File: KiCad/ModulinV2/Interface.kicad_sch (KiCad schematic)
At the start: 57 parts, among them IC10 DAC60501ZDGSR, IC11 DAC60501ZDGSR, IC4 TL072HIDR, IC5 TL074HIDR, IC51 TL072HIDR, IC6 ADS7041IDCUR, IC7 ADS7041IDCUR, IC8 ADS7866IDBVT, IC9 ADS7866IDBVT

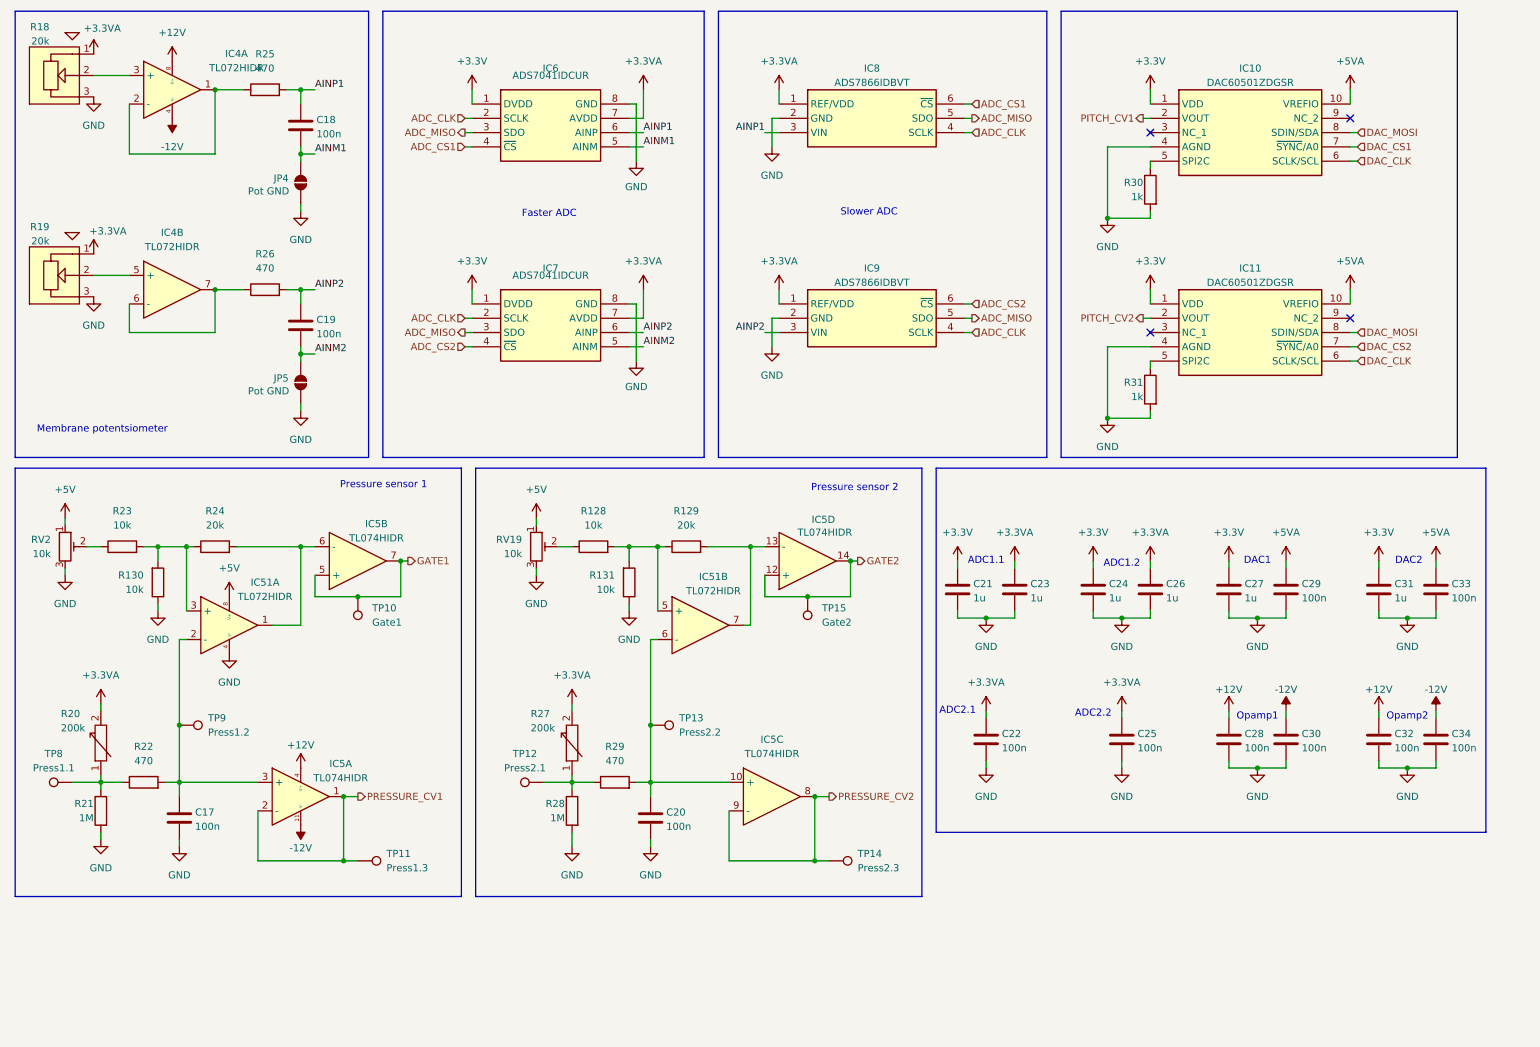
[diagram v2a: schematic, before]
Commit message: Started adding footprints for capacitors
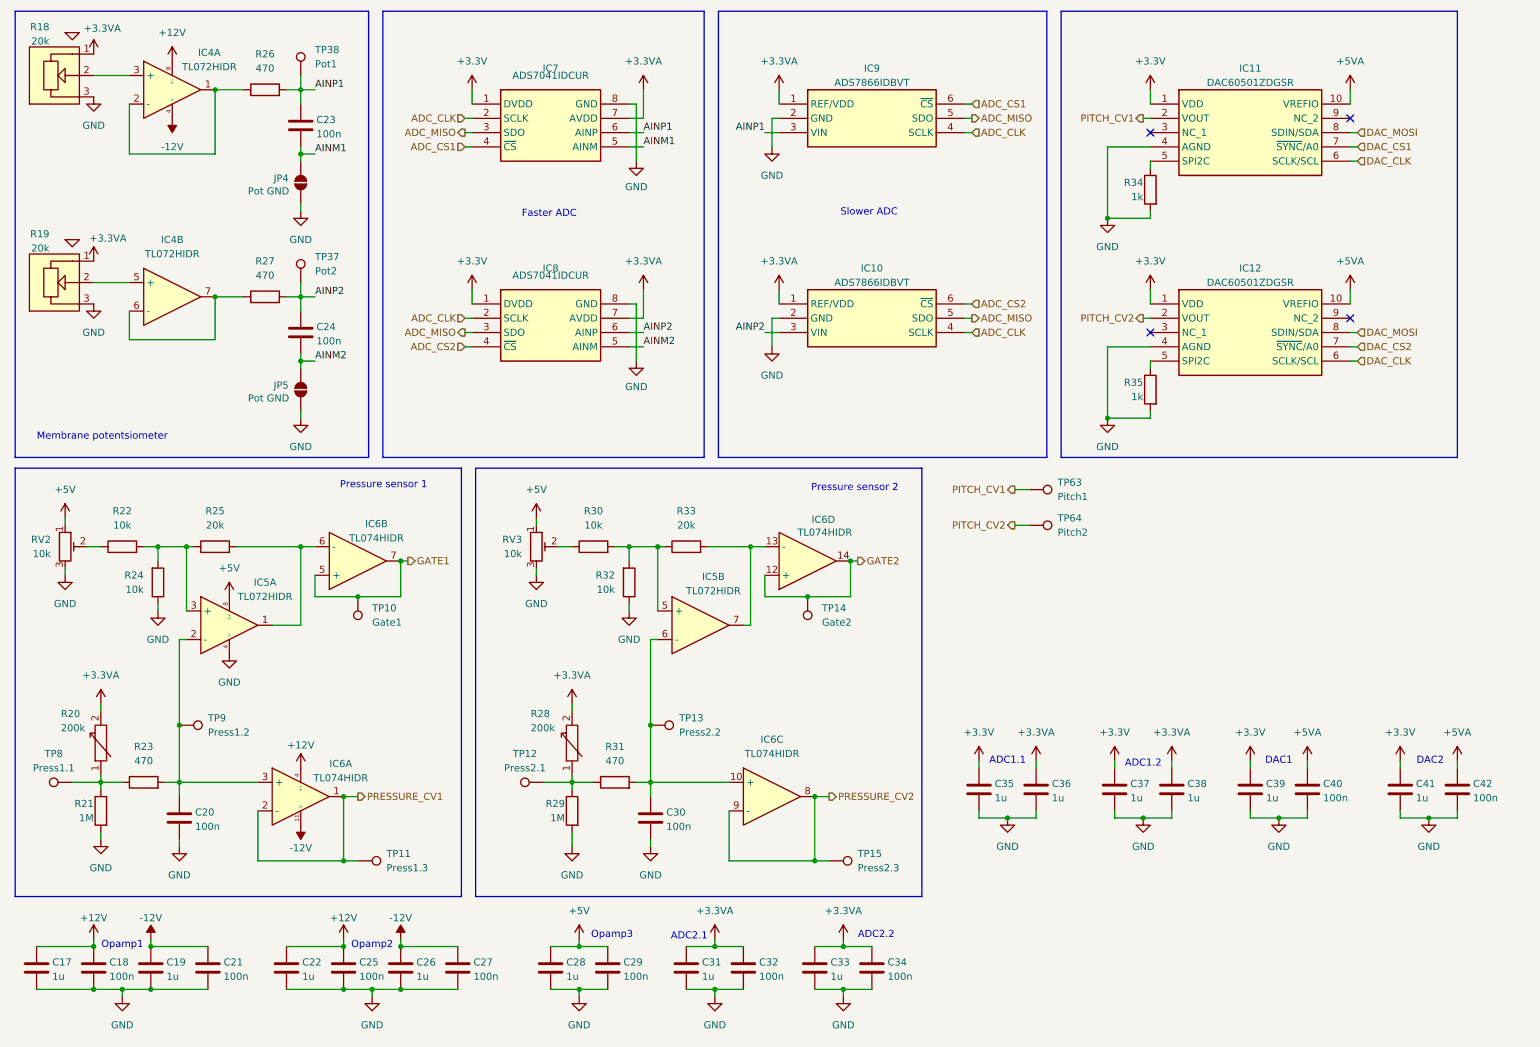
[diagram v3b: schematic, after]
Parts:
- removed C30, C34: 100n, symbol Device:C
- added C17, C19, C26, C31, C33: 1u, SamacSys_Parts:CAPC1608X95N, symbol Device:C
- added C18, C21, C25, C27, C29: 100n, SamacSys_Parts:CAPC1608X90N, symbol Device:C
- added TP37: Pot2, SamacSys_Parts:TestPointLoop, symbol Connector:TestPoint
- added TP38: Pot1, SamacSys_Parts:TestPointLoop, symbol Connector:TestPoint
- added TP63: Pitch1, SamacSys_Parts:TestPointLoop, symbol Connector:TestPoint
- added TP64: Pitch2, SamacSys_Parts:TestPointLoop, symbol Connector:TestPoint
- C20: renamed from C17; footprint (none) -> SamacSys_Parts:CAPC1608X90N
- C22, C28: value 100n -> 1u; footprint (none) -> SamacSys_Parts:CAPC1608X95N
- C23: renamed from C18; footprint (none) -> SamacSys_Parts:CAPC1608X90N
- C24: renamed from C19; footprint (none) -> SamacSys_Parts:CAPC1608X90N
- C30: renamed from C20; footprint (none) -> SamacSys_Parts:CAPC1608X90N
- C32: footprint (none) -> SamacSys_Parts:CAPC1608X90N
- C34: renamed from C25; footprint (none) -> SamacSys_Parts:CAPC1608X90N
- C35: renamed from C21; footprint (none) -> SamacSys_Parts:CAPC1608X95N
- C36: renamed from C23; footprint (none) -> SamacSys_Parts:CAPC1608X95N
- C37: renamed from C24; footprint (none) -> SamacSys_Parts:CAPC1608X95N
- C38: renamed from C26; footprint (none) -> SamacSys_Parts:CAPC1608X95N
- C39: renamed from C27; footprint (none) -> SamacSys_Parts:CAPC1608X95N
- C40: renamed from C29; footprint (none) -> SamacSys_Parts:CAPC1608X90N
- C41: renamed from C31; footprint (none) -> SamacSys_Parts:CAPC1608X95N
- C42: renamed from C33; footprint (none) -> SamacSys_Parts:CAPC1608X90N
- TP10, TP11, TP12, TP13, TP8, TP9: footprint (none) -> SamacSys_Parts:TestPointLoop
- TP14: renamed from TP15; footprint (none) -> SamacSys_Parts:TestPointLoop
- TP15: renamed from TP14; footprint (none) -> SamacSys_Parts:TestPointLoop
- renumbered IC9 to IC10, IC10 to IC11, IC11 to IC12, IC51 to IC5, IC5 to IC6, IC6 to IC7, IC7 to IC8, IC8 to IC9, R23 to R22, R22 to R23, R130 to R24, R24 to R25, R25 to R26, R26 to R27, R27 to R28, R28 to R29, R128 to R30, R29 to R31, R131 to R32, R129 to R33, R30 to R34, R31 to R35, RV19 to RV3
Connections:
- net +12V: now also C22.1, C17.1, C18.1, C25.1; no longer C28.1, C32.1
- net +3.3VA: now also C32.1, C31.1, C33.1; no longer C22.1
- net +5V: now also C28.1, C29.1
- net -12V: now also C19.1, C21.1, C26.1, C27.1
- net AINP1: now also TP38.1
- net AINP2: now also TP37.1
- net GND: now also C17.2, C18.2, C19.2, C21.2, C25.2, C26.2, C27.2, C29.2, C31.2, C33.2
- net PITCH_CV1: now also TP63.1
- net PITCH_CV2: now also TP64.1
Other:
- note added: "Opamp3"
- moved on the sheet: C24, C34, C35, C36, C37, C38, C39, C40, C41, C42, IC4B, JP5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

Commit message: Added footprints to all capacitors and potentiometers
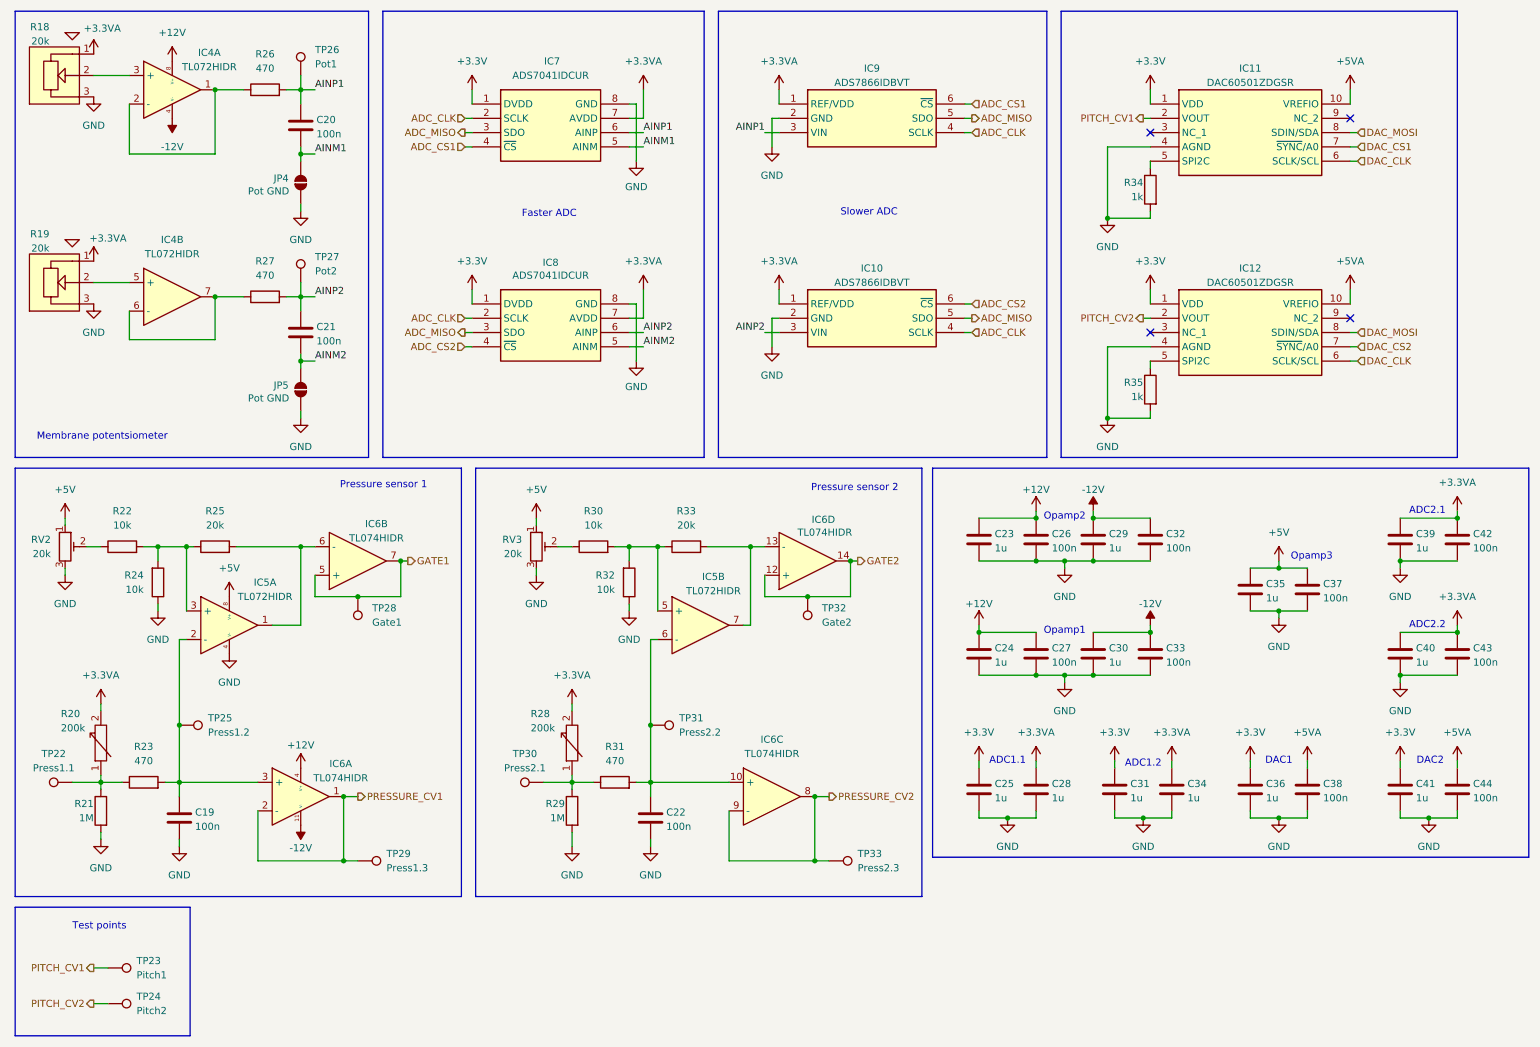
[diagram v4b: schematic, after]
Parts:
- C19: renamed from C20; footprint SamacSys_Parts:CAPC1608X90N -> Capacitor_SMD:C_0603_1608Metric_Pad1.08x0.95mm_HandSolder
- C20: renamed from C23; footprint SamacSys_Parts:CAPC1608X90N -> Capacitor_SMD:C_0603_1608Metric_Pad1.08x0.95mm_HandSolder
- C21: renamed from C24; footprint SamacSys_Parts:CAPC1608X90N -> Capacitor_SMD:C_0603_1608Metric_Pad1.08x0.95mm_HandSolder
- C22: renamed from C30; footprint SamacSys_Parts:CAPC1608X90N -> Capacitor_SMD:C_0603_1608Metric_Pad1.08x0.95mm_HandSolder
- C23: renamed from C22; footprint SamacSys_Parts:CAPC1608X95N -> Capacitor_SMD:C_0603_1608Metric_Pad1.08x0.95mm_HandSolder
- C24: renamed from C17; footprint SamacSys_Parts:CAPC1608X95N -> Capacitor_SMD:C_0603_1608Metric_Pad1.08x0.95mm_HandSolder
- C25: renamed from C35; footprint SamacSys_Parts:CAPC1608X95N -> Capacitor_SMD:C_0603_1608Metric_Pad1.08x0.95mm_HandSolder
- C26: renamed from C25; footprint SamacSys_Parts:CAPC1608X90N -> Capacitor_SMD:C_0603_1608Metric_Pad1.08x0.95mm_HandSolder
- C27: renamed from C18; footprint SamacSys_Parts:CAPC1608X90N -> Capacitor_SMD:C_0603_1608Metric_Pad1.08x0.95mm_HandSolder
- C28: renamed from C36; footprint SamacSys_Parts:CAPC1608X95N -> Capacitor_SMD:C_0603_1608Metric_Pad1.08x0.95mm_HandSolder
- C29: renamed from C26; footprint SamacSys_Parts:CAPC1608X95N -> Capacitor_SMD:C_0603_1608Metric_Pad1.08x0.95mm_HandSolder
- C30: renamed from C19; footprint SamacSys_Parts:CAPC1608X95N -> Capacitor_SMD:C_0603_1608Metric_Pad1.08x0.95mm_HandSolder
- C31: renamed from C37; footprint SamacSys_Parts:CAPC1608X95N -> Capacitor_SMD:C_0603_1608Metric_Pad1.08x0.95mm_HandSolder
- C32: renamed from C27; footprint SamacSys_Parts:CAPC1608X90N -> Capacitor_SMD:C_0603_1608Metric_Pad1.08x0.95mm_HandSolder
- C33: renamed from C21; footprint SamacSys_Parts:CAPC1608X90N -> Capacitor_SMD:C_0603_1608Metric_Pad1.08x0.95mm_HandSolder
- C34: renamed from C38; footprint SamacSys_Parts:CAPC1608X95N -> Capacitor_SMD:C_0603_1608Metric_Pad1.08x0.95mm_HandSolder
- C35: renamed from C28; footprint SamacSys_Parts:CAPC1608X95N -> Capacitor_SMD:C_0603_1608Metric_Pad1.08x0.95mm_HandSolder
- C36: renamed from C39; footprint SamacSys_Parts:CAPC1608X95N -> Capacitor_SMD:C_0603_1608Metric_Pad1.08x0.95mm_HandSolder
- C37: renamed from C29; footprint SamacSys_Parts:CAPC1608X90N -> Capacitor_SMD:C_0603_1608Metric_Pad1.08x0.95mm_HandSolder
- C38: renamed from C40; footprint SamacSys_Parts:CAPC1608X90N -> Capacitor_SMD:C_0603_1608Metric_Pad1.08x0.95mm_HandSolder
- C39: renamed from C31; footprint SamacSys_Parts:CAPC1608X95N -> Capacitor_SMD:C_0603_1608Metric_Pad1.08x0.95mm_HandSolder
- C40: renamed from C33; footprint SamacSys_Parts:CAPC1608X95N -> Capacitor_SMD:C_0603_1608Metric_Pad1.08x0.95mm_HandSolder
- C41: footprint SamacSys_Parts:CAPC1608X95N -> Capacitor_SMD:C_0603_1608Metric_Pad1.08x0.95mm_HandSolder
- C42: renamed from C32; footprint SamacSys_Parts:CAPC1608X90N -> Capacitor_SMD:C_0603_1608Metric_Pad1.08x0.95mm_HandSolder
- C43: renamed from C34; footprint SamacSys_Parts:CAPC1608X90N -> Capacitor_SMD:C_0603_1608Metric_Pad1.08x0.95mm_HandSolder
- C44: renamed from C42; footprint SamacSys_Parts:CAPC1608X90N -> Capacitor_SMD:C_0603_1608Metric_Pad1.08x0.95mm_HandSolder
- R18, R19: footprint TSP-L-0400-203-1%-ST:TSP-L-0400-203-1%-ST -> (none)
- RV2, RV3: value 10k -> 20k; footprint (none) -> SamacSys_Parts:PV36W201C01B00
- renumbered TP8 to TP22, TP63 to TP23, TP64 to TP24, TP9 to TP25, TP38 to TP26, TP37 to TP27, TP10 to TP28, TP11 to TP29, TP12 to TP30, TP13 to TP31, TP14 to TP32, TP15 to TP33
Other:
- note added: "Test points"
- moved on the sheet: C23, C24, C26, C27, C29, C30, C32, C33, C35, C37, C39, C40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

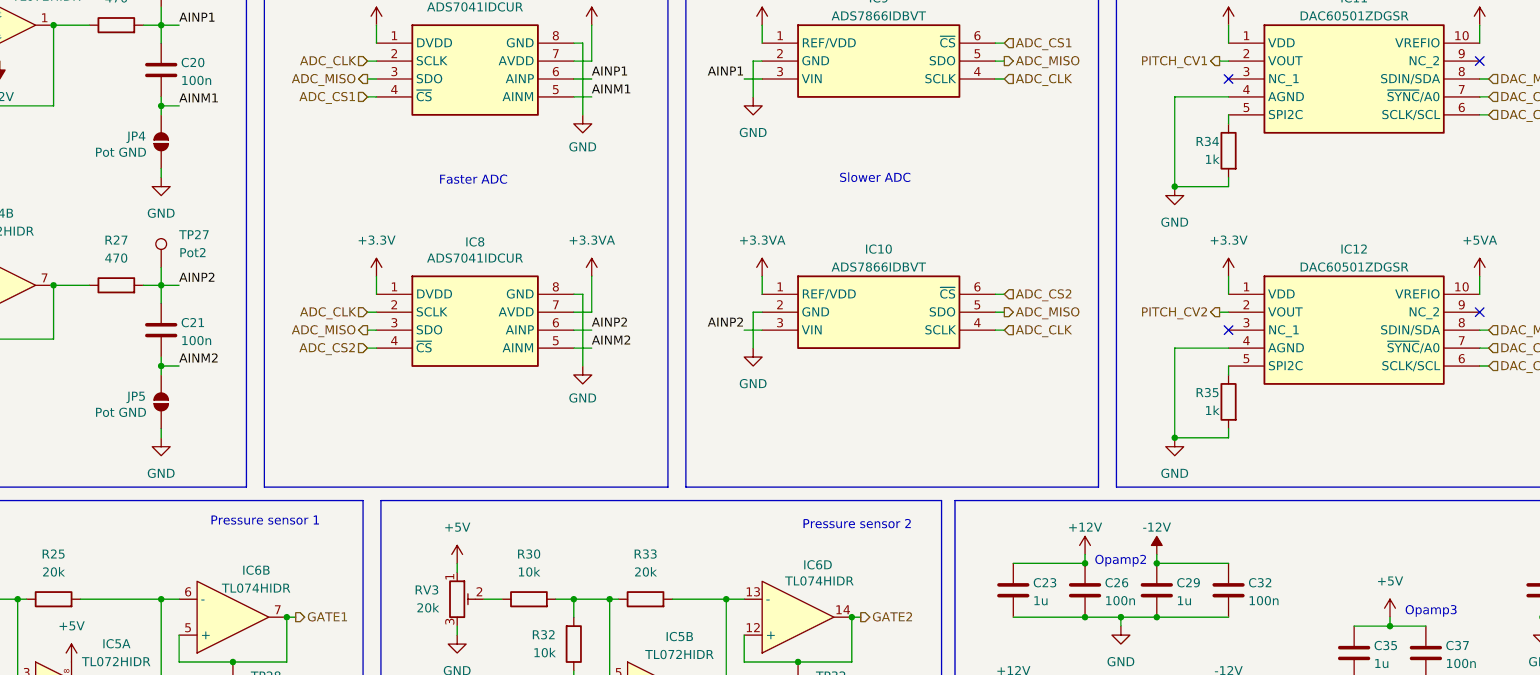
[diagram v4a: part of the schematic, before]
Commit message: Finished Schematic, started on PCB
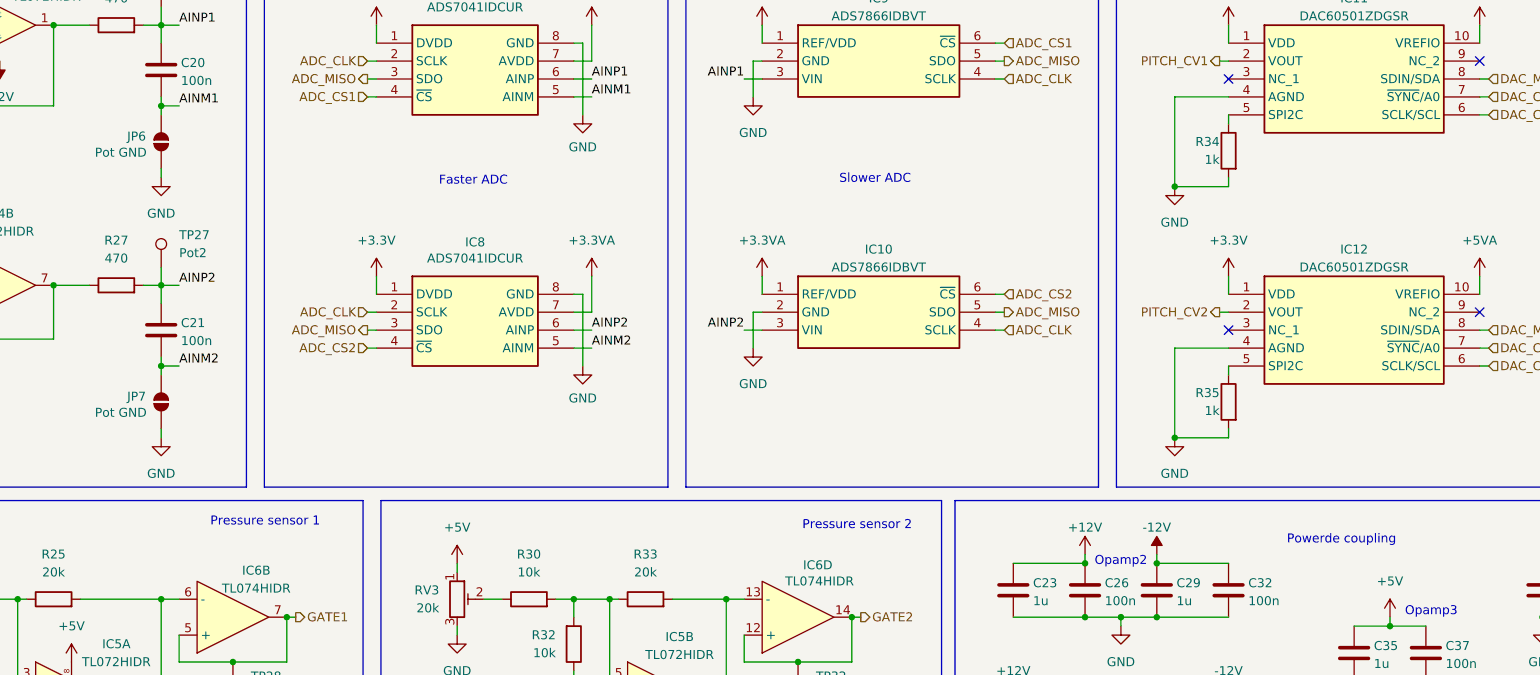
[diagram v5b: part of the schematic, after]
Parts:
- R18, R19: footprint (none) -> SamacSys_Parts:TSP-L-0400-203-1%-ST
- R20, R28: footprint (none) -> SamacSys_Parts:SEN0299
- R21, R22, R23, R24, R26, R27, R29, R30, R31, R32, R34, R35: footprint (none) -> Resistor_SMD:R_0603_1608Metric_Pad0.98x0.95mm_HandSolder
- R25, R33: footprint (none) -> Resistor_SMD:R_1206_3216Metric_Pad1.30x1.75mm_HandSolder
- renumbered JP4 to JP6, JP5 to JP7
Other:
- note added: "Powerde coupling"
